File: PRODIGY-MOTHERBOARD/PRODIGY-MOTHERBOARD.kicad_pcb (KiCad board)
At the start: 2 copper layers, 160 x 115 mm, 252 parts, among them J10 Neopixel, J11 Can, J12 USB_A, J13 SPI_OUT, J14 MOTOR, J15 12V OUT, J16 RTD_PT100, J17 SERIAL, J18 I2C, J19 KEYPAD_MATRIX, J2 USB_C_Receptacle, J21 DM3BT-DSF-PEJS/C, J3 Conn_02x20_Odd_Even, J5 Barrel_Jack_MountingPin, J6 USB_C_Receptacle, J8 Conn_02x20_Odd_Even, J9 A_IN, Q1 BC850, Q2 DMP2045U-7, Q3 BC850, Q4 BS870, Q5 BC850, Q6 ALS-PDIC15-21B/TR8, SW1 SW_Push, SW2 SW_Push, SW3 SW_Push, SW4 SW_Push, SW5 SW_Push, SW6 SW_Push, U1 TPS22810DRV, U10 PCF8574, U11 HDC1080, U12 LIS2DH12TR, U13 TXS0108EPW, U15 CC56-12YWA, U16 PN5321A3HN_C1xx, U17 IP4252CZ16, U18 CR2013-MI2120, U19 SN74LVC1T45DBV, U2 TPS54331DR, U20 TSDP341xx, U22 MCP6021RT-E/OT, U23 LMP2011, U24 LM4125AIM5-2.5, U25 LMP2011, U26 LMP2011, U27 LMP2011, U3 TPS54331DR, U4 TJA1051T-E, U5 DRV8870DDA, U6 PCA9306DC, U7 PCA9306DC, U8 SN74LVC1T45DBV, U9 PCF8574

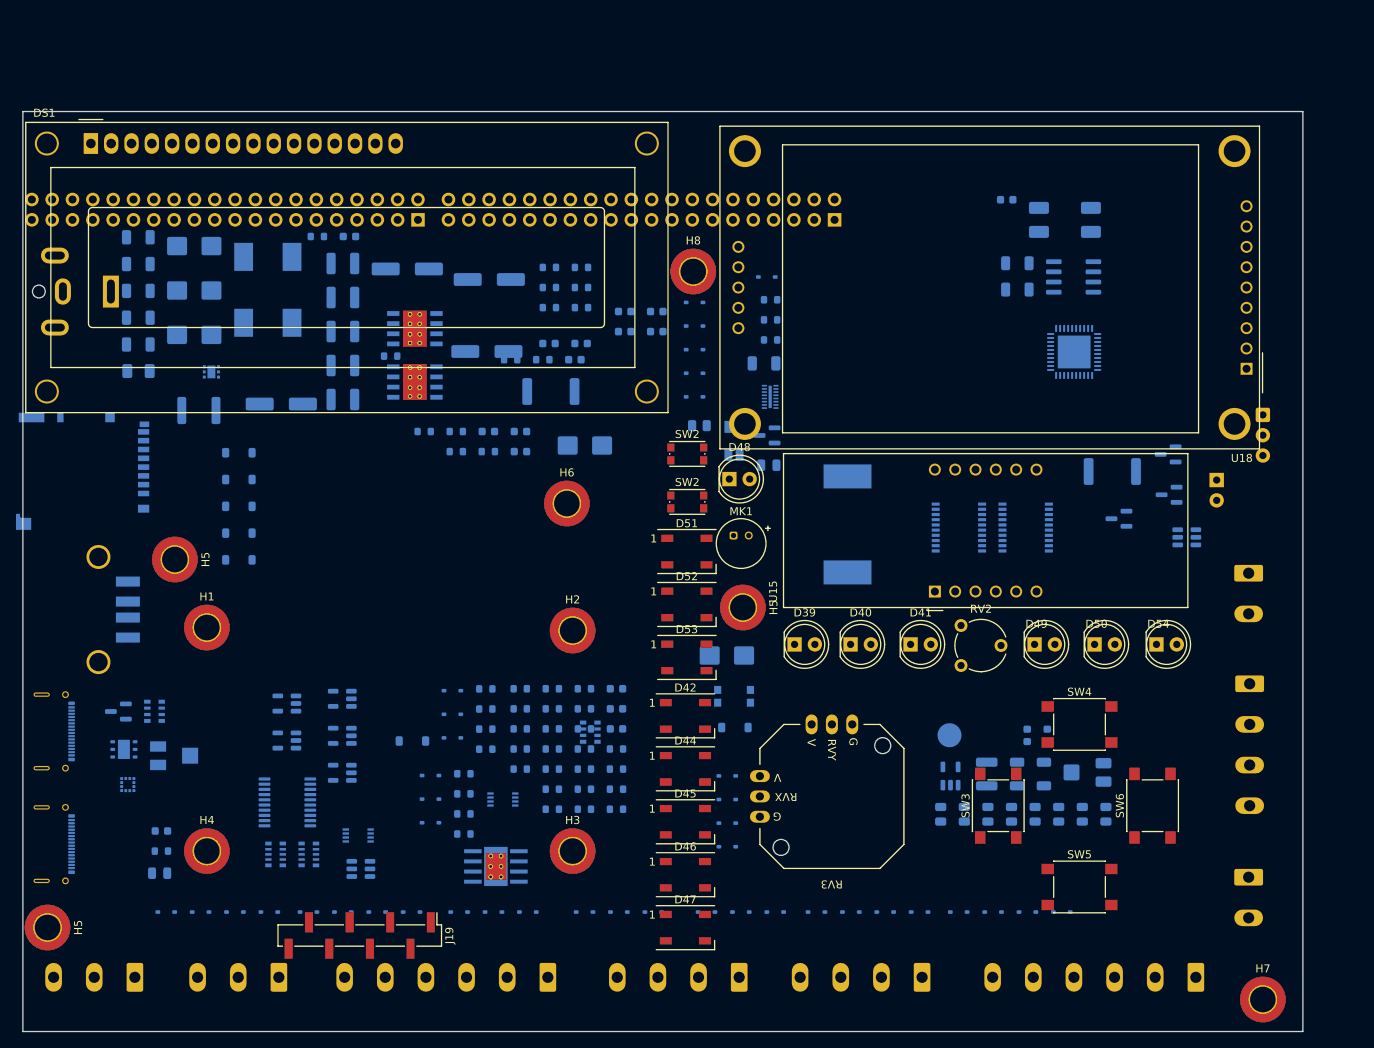
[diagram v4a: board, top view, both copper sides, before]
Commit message: MBT Schematic improved
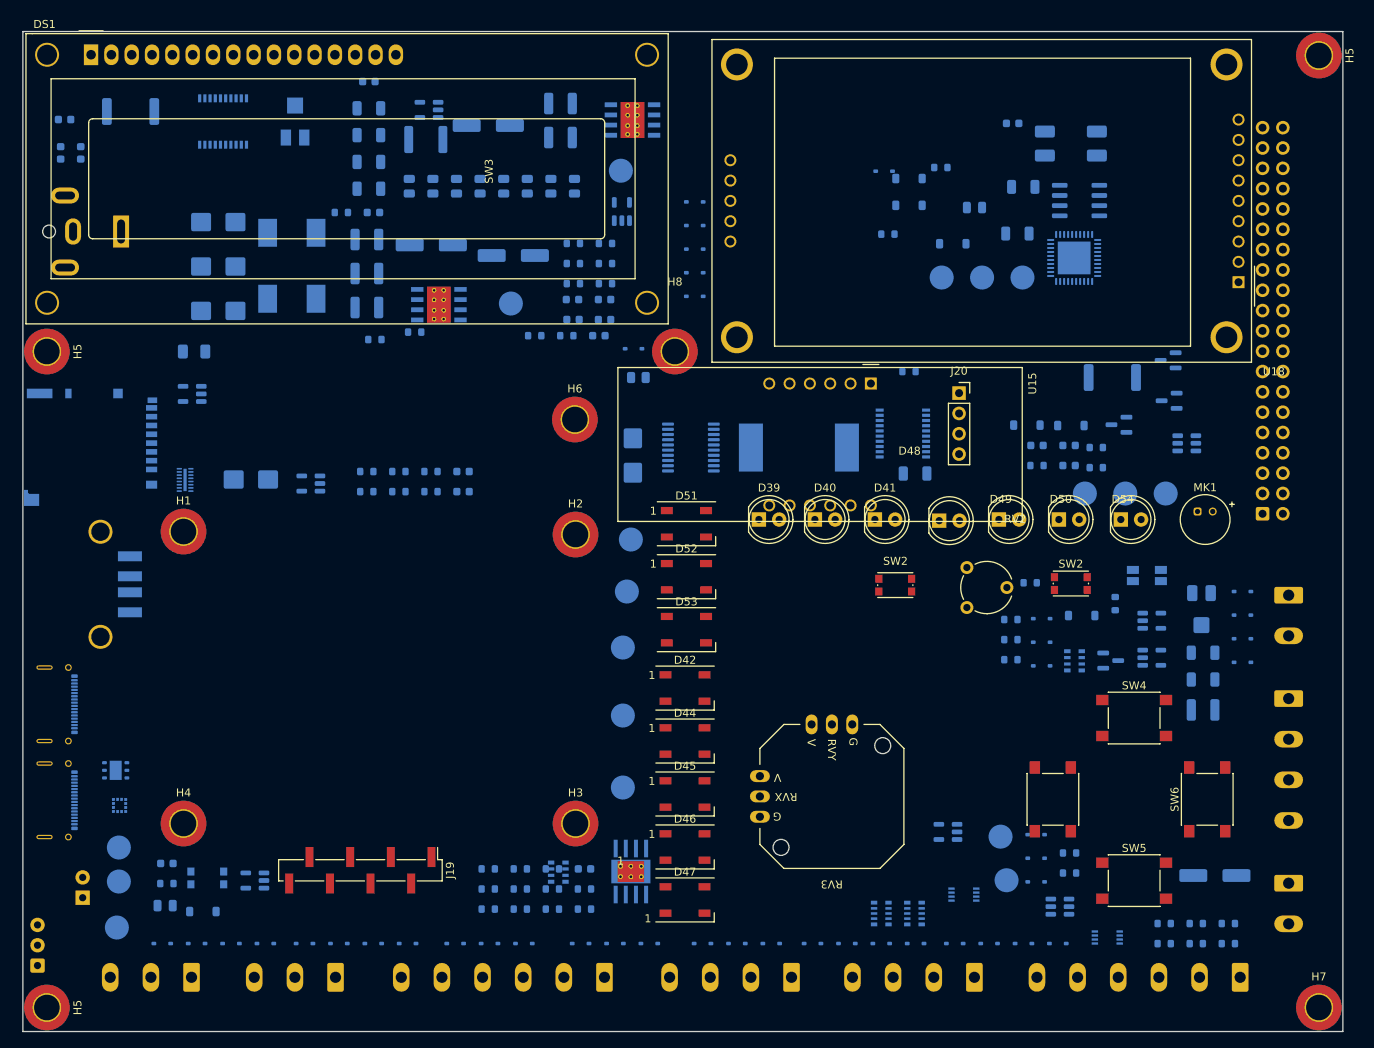
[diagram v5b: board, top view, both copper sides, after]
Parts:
- removed C3: 22nF, Capacitor_SMD:C_0603_1608Metric
- removed C65: 10uF, Capacitor_SMD:C_1206_3216Metric
- removed J21: DM3BT-DSF-PEJS/C, Connector_Card:microSD_HC_Hirose_DM3BT-DSF-PEJS
- removed J8: Conn_02x20_Odd_Even, Connector_PinHeader_2.54mm:PinHeader_2x20_P2.54mm_Horizontal
- removed Q2: DMP2045U-7, Package_TO_SOT_SMD:SOT-23
- removed R38, R39: 10k, Resistor_SMD:R_0603_1608Metric
- removed U17: IP4252CZ16, Package_SON:Nexperia_HUSON-16_USON-16-1EP_1.35x3.3mm_P0.4mm_EP0.4x2.8mm
- added C92: 100nF, Capacitor_SMD:C_0805_2012Metric, B.Cu at (186.9, 42.0)
- added J20: OLED, Connector_PinSocket_2.54mm:PinSocket_1x04_P2.54mm_Vertical, F.Cu at (185.0, 65.2)
- added J22: DM3BT-DSF-PEJS/C, Connector_Card:microSD_HC_Hirose_DM3BT-DSF-PEJS, B.Cu at (76.5, 72.0)
- added R88: 10k, Resistor_SMD:R_0603_1608Metric, B.Cu at (182.7, 37.0)
- added TP10: ~, TestPoint:TestPoint_Pad_D3.0mm, B.Cu at (190.2, 120.6)
- added TP11: ~, TestPoint:TestPoint_Pad_D3.0mm, B.Cu at (137.0, 83.0)
- added TP12: ~, TestPoint:TestPoint_Pad_D3.0mm, B.Cu at (191.0, 126.1)
- added TP13: ~, TestPoint:TestPoint_Pad_D3.0mm, B.Cu at (143.0, 97.0)
- added TP14: ~, TestPoint:TestPoint_Pad_D3.0mm, B.Cu at (129.0, 54.0)
- added TP15: ~, TestPoint:TestPoint_Pad_D3.0mm, B.Cu at (80.0, 122.0)
- added TP16: ~, TestPoint:TestPoint_Pad_D3.0mm, B.Cu at (80.0, 126.2)
- added TP2: ~, TestPoint:TestPoint_Pad_D3.0mm, B.Cu at (182.8, 50.8)
- added TP20: ~, TestPoint:TestPoint_Pad_D3.0mm, B.Cu at (143.0, 105.5)
- added TP21: ~, TestPoint:TestPoint_Pad_D3.0mm, B.Cu at (143.0, 114.5)
- added TP22: ~, TestPoint:TestPoint_Pad_D3.0mm, B.Cu at (144.0, 83.5)
- added TP3: ~, TestPoint:TestPoint_Pad_D3.0mm, B.Cu at (187.9, 50.8)
- added TP4: ~, TestPoint:TestPoint_Pad_D3.0mm, B.Cu at (192.9, 50.8)
- added TP5: ~, TestPoint:TestPoint_Pad_D3.0mm, B.Cu at (79.8, 132.0)
- added TP6: ~, TestPoint:TestPoint_Pad_D3.0mm, B.Cu at (200.8, 77.8)
- added TP7: ~, TestPoint:TestPoint_Pad_D3.0mm, B.Cu at (205.8, 77.8)
- added TP8: ~, TestPoint:TestPoint_Pad_D3.0mm, B.Cu at (210.8, 77.8)
- added TP9: ~, TestPoint:TestPoint_Pad_D3.0mm, B.Cu at (143.5, 90.0)
- added U29: IP4252CZ16, Package_SON:Nexperia_HUSON-16_USON-16-1EP_1.35x3.3mm_P0.4mm_EP0.4x2.8mm, B.Cu at (88.3, 76.0)
- added U30: RT9742AGJ5F, Package_TO_SOT_SMD:TSOT-23-5, B.Cu at (89.2, 65.3)
- C2: value 4.7uF -> 100nF; footprint Capacitor_SMD:C_1206_3216Metric -> Capacitor_SMD:C_0603_1608Metric
- C66: value 100nF -> 10uF; footprint Capacitor_SMD:C_0805_2012Metric -> Capacitor_SMD:C_1206_3216Metric
- J3: footprint Connector_PinHeader_2.54mm:PinHeader_2x20_P2.54mm_Horizontal -> Connector_IDC:IDC-Header_2x20_P2.54mm_Horizontal
- L2, L3: value 6.8 -> 6.8uH
- R40: value 100 -> DNP
- R5: value DNP -> 10k
- U1: value TPS22810DRV -> RT9742AGJ5F; footprint Package_SON:WSON-6-1EP_2x2mm_P0.65mm_EP1x1.6mm -> Package_TO_SOT_SMD:TSOT-23-5
- moved U20 167.9 mm to (69.8, 136.8), turned to 90 degrees
- moved H5 156.3 mm to (230.0, 23.0)
- moved D43 151.1 mm to (75.5, 128.3), turned to 90 degrees
- moved C85 141.1 mm to (75.2, 35.2)
- moved C86 141.1 mm to (72.7, 35.2)
- moved Q1 124.2 mm to (204.0, 98.6), turned to 0 degrees
- moved RN2 115.2 mm to (199.5, 98.7), turned to 0 degrees
- moved U9 112.4 mm to (93.0, 31.2), turned to -90 degrees
- moved C22 112.1 mm to (217.0, 125.5)
- moved J3 111.8 mm to (223.0, 80.3), turned to 0 degrees
- moved D58 104.2 mm to (199.0, 69.2)
- moved R72 102.8 mm to (136.9, 39.3)
- moved R73 102.8 mm to (134.0, 39.3)
- moved R75 102.8 mm to (128.1, 39.3)
- moved R76 102.8 mm to (125.2, 39.3)
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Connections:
- C2 pad 1: +5V -> /OUTPUTS/BREAKOUT_USB_VBUS
- C66 pad 1: /SPI/micro_SD/SD_VCC -> /SD/SD_VCC
- D66 pad 2: +3V3 -> +3.3VA
- Q6 pad 1: +3V3 -> +3.3VA
- Q6 pad 3: +3V3 -> +3.3VA
- R40 pad 2: /MCU/SPI_ENABLE_SD -> +3.3V
- R5 pad 1: Net-(U1-QOD) -> GND
- R5 pad 2: /OUTPUTS/BREAKOUT_USB_VBUS -> /MCU/USB_HOST_ENABLE
- RN3 pad 6: /SPI/CS_SD -> unconnected-(RN3-R5-Pad6)
- RV2 pad 3: +3V3 -> +3.3VA
- RV3 pad 1: +3V3 -> +3.3VA
- RV3 pad 4: +3V3 -> +3.3VA
- TH1 pad 1: +3V3 -> +3.3VA
- U1 pad 2: Net-(U1-QOD) -> GND
- U1 pad 3: Net-(U1-CT) -> /MCU/USB_HOST_FAULT
- U1 pad 4: GND -> /MCU/USB_HOST_ENABLE
- U1 pad 5: /MCU/USB_HOST_ENABLE -> +5V
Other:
- board size 160 x 115 mm -> 165 x 125 mm

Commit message: schematic v0.2 finalized
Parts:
- removed C92: 100nF, Capacitor_SMD:C_0805_2012Metric
- removed the H5 at (230.0, 23.0)
- removed the H5 at (71.0, 60.0)
- removed J22: DM3BT-DSF-PEJS/C, Connector_Card:microSD_HC_Hirose_DM3BT-DSF-PEJS
- removed Q6: ALS-PDIC15-21B/TR8, OptoDevice:Kingbright_KPS-3227
- removed R88: 10k, Resistor_SMD:R_0603_1608Metric
- removed TP20, TP21, TP22: ~, TestPoint:TestPoint_Pad_D3.0mm
- removed U29: IP4252CZ16, Package_SON:Nexperia_HUSON-16_USON-16-1EP_1.35x3.3mm_P0.4mm_EP0.4x2.8mm
- removed U30: RT9742AGJ5F, Package_TO_SOT_SMD:TSOT-23-5
- added C26: 100nF, Capacitor_SMD:C_0603_1608Metric, B.Cu at (99.6, 114.5)
- added C3: 100uF, Capacitor_SMD:CP_Elec_6.3x7.7, B.Cu at (97.0, 125.7)
- added C32: 47uF, Capacitor_SMD:CP_Elec_6.3x5.8, B.Cu at (110.2, 66.5)
- added C41: 10uF, Capacitor_SMD:C_0805_2012Metric, B.Cu at (90.1, 112.2)
- added C73: 4.7uF, Capacitor_SMD:C_0603_1608Metric, B.Cu at (99.6, 93.2)
- added C75: 4.7uF, Capacitor_SMD:C_0603_1608Metric, B.Cu at (99.6, 95.7)
- added C82: 1uF, Capacitor_SMD:C_0603_1608Metric, B.Cu at (119.7, 101.2)
- added C83: 100nF, Capacitor_SMD:C_0603_1608Metric, B.Cu at (119.7, 103.7)
- added C84: 100nF C0G, Capacitor_SMD:C_1206_3216Metric, B.Cu at (118.8, 93.6)
- added C90: 100nF, Capacitor_SMD:C_0805_2012Metric, B.Cu at (130.3, 113.2)
- added H10: MountingHole, MountingHole:MountingHole_3.2mm_M3_ISO7380_Pad_TopBottom, F.Cu at (230.0, 23.0)
- added H9: MountingHole, MountingHole:MountingHole_3.2mm_M3_ISO7380_Pad_TopBottom, F.Cu at (71.0, 60.0)
- added J21: DM3BT-DSF-PEJS/C, Connector_Card:microSD_HC_Hirose_DM3BT-DSF-PEJS, B.Cu at (76.5, 115.0)
- added Q2: BC850, Package_TO_SOT_SMD:SOT-23, B.Cu at (95.1, 94.3)
- added R38: 10k, Resistor_SMD:R_0603_1608Metric, B.Cu at (99.6, 98.2)
- added R39: 4.7k, Resistor_SMD:R_0603_1608Metric, B.Cu at (99.6, 100.7)
- added R69: 1k, Resistor_SMD:R_0805_2012Metric, B.Cu at (123.9, 93.4)
- added R70: 1k, Resistor_SMD:R_0805_2012Metric, B.Cu at (123.9, 96.3)
- added R71: 68k, Resistor_SMD:R_0805_2012Metric, B.Cu at (123.9, 99.3)
- added R85: DNP, Resistor_SMD:R_0603_1608Metric, B.Cu at (134.5, 113.0)
- added R86: 10k, Resistor_SMD:R_0603_1608Metric, B.Cu at (134.5, 115.5)
- added RN5: 10k, Resistor_SMD:R_Array_Convex_4x0603, B.Cu at (90.2, 106.3)
- added TP17: ~, TestPoint:TestPoint_Pad_D3.0mm, B.Cu at (120.0, 62.0)
- added TP18: ~, TestPoint:TestPoint_Pad_D3.0mm, B.Cu at (125.0, 62.0)
- added TP19: ~, TestPoint:TestPoint_Pad_D3.0mm, B.Cu at (130.1, 62.0)
- added U17: CR2013-MI2120, Display:CR2013-MI2120, F.Cu at (155.0, 30.3)
- added U21: MCP6021RT-E/OT, Package_TO_SOT_SMD:SOT-23-5, B.Cu at (119.1, 97.7)
- added U28: RT9742AGJ5F, Package_TO_SOT_SMD:TSOT-23-5, B.Cu at (134.0, 109.5)
- C11: value 100nF -> 10nF
- C13: value 10nF -> 1nF
- C14: value 1nF -> 4.7nF
- C15: value 4.7nF -> 47pF
- C16: value 47pF -> 39pF
- C17: value 39pF -> 100nF
- C19, C2: value 100nF -> 47uF; footprint Capacitor_SMD:C_0603_1608Metric -> Capacitor_SMD:C_1210_3225Metric
- C21: footprint Capacitor_SMD:C_1210_3225Metric -> Capacitor_SMD:CP_Elec_6.3x5.8
- C23: footprint Capacitor_SMD:CP_Elec_6.3x5.8 -> Capacitor_SMD:C_1210_3225Metric
- C4: value 100uF -> 100nF; footprint Capacitor_SMD:CP_Elec_6.3x7.7 -> Capacitor_SMD:C_0603_1608Metric
- C42: value 10uF -> 100nF; footprint Capacitor_SMD:C_0805_2012Metric -> Capacitor_SMD:C_0603_1608Metric
- C5: value 47uF -> 4.7uF; footprint Capacitor_SMD:C_1210_3225Metric -> Capacitor_SMD:C_1206_3216Metric
- C85: value 1uF -> 47uF; footprint Capacitor_SMD:C_0603_1608Metric -> Capacitor_SMD:C_1210_3225Metric
- C86: value 100nF -> 10uF; footprint Capacitor_SMD:C_0603_1608Metric -> Capacitor_SMD:C_1206_3216Metric
- C9: value 4.7uF -> 100nF; footprint Capacitor_SMD:C_1206_3216Metric -> Capacitor_SMD:C_0603_1608Metric
- D56: value 1N4148W -> SD05_SOD323; footprint Diode_SMD:D_SOD-123 -> Diode_SMD:D_SOD-323
- D57: value SD05_SOD323 -> 1N4148W; footprint Diode_SMD:D_SOD-323 -> Diode_SMD:D_SOD-123
- J10: value Neopixel -> RTD_PT100; footprint Connector_Phoenix_MSTB:PhoenixContact_MSTBA_2,5_3-G-5,08_1x03_P5.08mm_Horizontal -> Connector_Phoenix_MSTB:PhoenixContact_MSTBA_2,5_4-G-5,08_1x04_P5.08mm_Horizontal
- J16: value RTD_PT100 -> Neopixel; footprint Connector_Phoenix_MSTB:PhoenixContact_MSTBA_2,5_4-G-5,08_1x04_P5.08mm_Horizontal -> Connector_Phoenix_MSTB:PhoenixContact_MSTBA_2,5_3-G-5,08_1x03_P5.08mm_Horizontal
- Q3: value BC850 -> BS870
- Q4: value BS870 -> BC850
- Q5: value BC850 -> ALS-PDIC15-21B/TR8; footprint Package_TO_SOT_SMD:SOT-23 -> OptoDevice:Kingbright_KPS-3227
- R40: value DNP -> 1k
- R41: value 10k -> 100
- R42: value 4.7k -> 39
- R44: value 100 -> 1k
- R45: value 39 -> 1k
- R46, R48, R56, R60, R61: value 1k -> 10k
- R47, R72: value 1k -> 100
- R49: value 10k -> 22; footprint Resistor_SMD:R_0603_1608Metric -> Resistor_SMD:R_2512_6332Metric
- R50: value 100 -> 10k
- R52: value 22 -> 10k; footprint Resistor_SMD:R_2512_6332Metric -> Resistor_SMD:R_0603_1608Metric
- R54, R57, R58, R59: value 10k -> 1k
- R73: value 1k -> 220k
- R74: value 68k -> 220k
- R75: value 100 -> 220k
- R76: value 220k -> 1k
- RN3, RN4: footprint Resistor_SMD:R_Array_Convex_5x0603 -> Resistor_SMD:R_Array_Convex_4x0603
- TP1: value A1 -> ~
- TP16: value ~ -> A1
- U18: value CR2013-MI2120 -> SN74LVC1T45DBV; footprint Display:CR2013-MI2120 -> Package_TO_SOT_SMD:SOT-23-6; moved to B.Cu
- U19: value SN74LVC1T45DBV -> TSDP341xx; footprint Package_TO_SOT_SMD:SOT-23-6 -> OptoDevice:Vishay_MOLD-3Pin
- U22: value MCP6021RT-E/OT -> LMP2011; footprint Package_TO_SOT_SMD:SOT-23-5 -> Package_TO_SOT_SMD:TSOT-23-5
- U23: value LMP2011 -> LM4125AIM5-2.5; footprint Package_TO_SOT_SMD:TSOT-23-5 -> Package_TO_SOT_SMD:SOT-23-5
- U24: value LM4125AIM5-2.5 -> LMP2011; footprint Package_TO_SOT_SMD:SOT-23-5 -> Package_TO_SOT_SMD:TSOT-23-5
- U27: value LMP2011 -> IP4252CZ16; footprint Package_TO_SOT_SMD:TSOT-23-5 -> Package_SON:Nexperia_HUSON-16_USON-16-1EP_1.35x3.3mm_P0.4mm_EP0.4x2.8mm
- moved U18 110.0 mm to (124.7, 106.2), turned to 0 degrees
- moved TP16 71.8 mm to (82.0, 54.5)
- moved TP5 71.8 mm to (81.8, 60.2)
- moved TP15 44.8 mm to (85.5, 77.5)
- moved U12 41.9 mm to (80.5, 74.9)
- moved U11 41.9 mm to (80.0, 70.5)
- moved J2 34.6 mm to (71.5, 81.5)
- moved J6 34.6 mm to (71.5, 69.5)
- moved R45 26.0 mm to (93.5, 70.0)
- moved R46 26.0 mm to (93.5, 72.5)
- moved C76 26.0 mm to (97.5, 70.0)
- moved C78 26.0 mm to (97.5, 72.5)
- moved D3 18.3 mm to (81.8, 65.0)
- moved R53 18.3 mm to (100.3, 64.0)
- moved R54 18.3 mm to (100.3, 66.5)
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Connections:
- C10 pad 1: +12V -> +5V
- C11 pad 1: +5V -> Net-(U2-SS)
- C12 pad 1: Net-(U2-SS) -> Net-(U3-SS)
- C13 pad 1: Net-(U3-SS) -> Net-(U2-COMP)
- C13 pad 2: GND -> Net-(C13-Pad2)
- C14 pad 1: Net-(U2-COMP) -> Net-(U3-COMP)
- C15 pad 1: Net-(U3-COMP) -> Net-(U2-COMP)
- C15 pad 2: Net-(C15-Pad2) -> GND
- C16 pad 1: Net-(U2-COMP) -> Net-(U3-COMP)
- C17 pad 1: Net-(U3-COMP) -> Net-(U2-BOOT)
- C17 pad 2: GND -> Net-(D7-K)
- C18 pad 1: Net-(U2-BOOT) -> Net-(U3-BOOT)
- C18 pad 2: Net-(D7-K) -> Net-(D8-K)
- C19 pad 1: Net-(U3-BOOT) -> +3V3
- C19 pad 2: Net-(D8-K) -> GND
- C20 pad 1: +3V3 -> +5V
- C21 pad 1: +5V -> +3V3
- C22 pad 1: +3V3 -> +5V
- C23 pad 1: +5V -> +3V3
- C24 pad 1: +3V3 -> +5V
- C4 pad 1: +12V -> /OUTPUTS/BREAKOUT_USB_VBUS
- C5 pad 1: /OUTPUTS/BREAKOUT_USB_VBUS -> +12V
- C6 pad 1: +12V -> +5V
- C7 pad 1: +5V -> +12V
- C76 pad 1: /MCU/DIGITAL_BUTTON_IN_2 -> /MCU/DIGITAL_BUTTON_IN_1
- C8 pad 1: +12V -> +5V
- C85 pad 1: +3.3VA -> Net-(C84-Pad1)
- C85 pad 2: GND -> Net-(U21-+)
- C86 pad 1: +3.3VA -> Net-(U21--)
- C86 pad 2: GND -> Net-(C86-Pad2)
- C89 pad 1: Net-(U22--) -> /SD/SD_VCC
- C89 pad 2: Net-(C89-Pad2) -> GND
- C9 pad 1: +5V -> +12V
- D14 pad 2: /CAN/CAN_H -> /OUTPUTS/RTD_W1
- D15 pad 2: /OUTPUTS/BREAKOUT_NEOPIXEL_IN -> /OUTPUTS/RTD_W2
- D16 pad 2: /50Hz Filter/IN_P1+ -> /CAN/CAN_H
- D17 pad 2: /CAN/CAN_L -> /OUTPUTS/RTD_W3
- D18 pad 2: /50Hz Filter/IN_P1- -> /50Hz Filter/IN_P1+
- D19 pad 2: /SPI/CS_BREAKOUT -> /CAN/CAN_L
- D20 pad 2: /OUTPUTS/BREAKOUT_USB_VBUS -> /OUTPUTS/RTD_W4
- D21 pad 2: /MOTOR/MOTOR_OUT1_BREAKOUT_1 -> /50Hz Filter/IN_P1-
- D22 pad 2: /SPI/CLK -> /SPI/CS_BREAKOUT
- D23 pad 2: /MCU/USB_HOST_OUT_P+ -> /OUTPUTS/BREAKOUT_USB_VBUS
- D24 pad 2: /MCU/MOTOR_CC_IN_1 -> /MOTOR/MOTOR_OUT1_BREAKOUT_1
- D25 pad 2: /SPI/MISO -> /SPI/CLK
- D26 pad 2: /MCU/USB_HOST_OUT_P- -> /MCU/USB_HOST_OUT_P+
- D27 pad 2: /MCU/MOTOR_CC_IN_2 -> /MCU/MOTOR_CC_IN_1
- D28 pad 2: /SPI/MOSI -> /SPI/MISO
- D29 pad 2: /MOTOR/MOTOR_OUT2_BREAKOUT_1 -> /MCU/USB_HOST_OUT_P-
- D30 pad 2: /OUTPUTS/RTD_W1 -> /MCU/MOTOR_CC_IN_2
- D31 pad 2: +12V -> /SPI/CLK
- D32 pad 2: /OUTPUTS/RTD_W2 -> /MOTOR/MOTOR_OUT2_BREAKOUT_1
- D33 pad 2: /OUTPUTS/RTD_W3 -> +12V
- D34 pad 2: /OUTPUTS/RTD_W4 -> /OUTPUTS/BREAKOUT_NEOPIXEL_IN
- D56 pad 1: /MCU/DIGITAL_BUTTON_IN_2 -> GND
- D56 pad 2: Net-(D55-A2) -> Net-(D56-A2)
- D57 pad 1: GND -> Net-(D57-K)
- D57 pad 2: Net-(D57-A2) -> Net-(D56-A2)
- D58 pad 1: Net-(D58-K) -> /MCU/DIGITAL_BUTTON_IN_2
- D58 pad 2: Net-(D57-A2) -> Net-(D55-A2)
- J10 pad 1: /OUTPUTS/BREAKOUT_NEOPIXEL_IN -> /OUTPUTS/RTD_W1
- J10 pad 2: +5V -> /OUTPUTS/RTD_W2
- J10 pad 3: GND -> /OUTPUTS/RTD_W3
- J13 pad 4: /SPI/MOSI -> /SPI/CLK
- J16 pad 1: /OUTPUTS/RTD_W1 -> /OUTPUTS/BREAKOUT_NEOPIXEL_IN
- J16 pad 2: /OUTPUTS/RTD_W2 -> +5V
- J16 pad 3: /OUTPUTS/RTD_W3 -> GND
- Q3 pad 1: Net-(Q3-B) -> Net-(Q3-G)
- Q3 pad 3: Net-(D43-K) -> Net-(D54-K)
- Q4 pad 1: Net-(Q4-G) -> Net-(Q4-B)
- Q4 pad 3: Net-(D54-K) -> Net-(BZ1-+)
- Q5 pad 1: Net-(Q5-B) -> +3.3VA
- Q5 pad 2: GND -> /MCU/ANALOG_PHOTOTRANSISTOR
- Q5 pad 3: Net-(BZ1-+) -> +3.3VA
- R10 pad 1: Net-(C14-Pad2) -> Net-(C13-Pad2)
- R11 pad 1: Net-(C15-Pad2) -> Net-(C14-Pad2)
- R40 pad 1: Net-(R40-Pad1) -> GND
- R40 pad 2: +3.3V -> Net-(D41-K)
- R41 pad 1: GND -> /MCU/DIGITAL_IR_EMITTER
- R41 pad 2: Net-(D39-K) -> Net-(Q2-B)
- R42 pad 1: GND -> Net-(D43-A)
- R42 pad 2: Net-(D40-K) -> +3V3
- R43 pad 2: Net-(D41-K) -> Net-(D48-K)
- R44 pad 1: /MCU/DIGITAL_IR_EMITTER -> GND
- R44 pad 2: Net-(Q3-B) -> Net-(D49-K)
- R45 pad 1: Net-(D43-A) -> GND
- R45 pad 2: +3V3 -> Net-(D50-K)
- R46 pad 2: Net-(D48-K) -> /MCU/DIGITAL_HEATER_OUT
- R47 pad 1: GND -> /MCU/DIGITAL_HEATER_OUT
- R47 pad 2: Net-(D49-K) -> Net-(Q3-G)
- R48 pad 1: GND -> Net-(D54-A)
- R48 pad 2: Net-(D50-K) -> +12V
- R49 pad 1: GND -> Net-(F2-Pad2)
- R49 pad 2: /MCU/DIGITAL_HEATER_OUT -> Net-(D54-K)
- R50 pad 1: /MCU/DIGITAL_HEATER_OUT -> Net-(D55-A2)
- R50 pad 2: Net-(Q4-G) -> +3V3
- R51 pad 1: Net-(D54-A) -> Net-(D56-A2)
- R51 pad 2: +12V -> +3V3
- R52 pad 1: Net-(F2-Pad2) -> Net-(D56-A2)
- R52 pad 2: Net-(D54-K) -> Net-(D57-K)
- R53 pad 2: +3V3 -> /MCU/DIGITAL_BUTTON_IN_2
- R54 pad 1: Net-(D57-A2) -> /MCU/DIGITAL_BUZZER_OUT
- R54 pad 2: +3V3 -> Net-(Q4-B)
- R55 pad 1: Net-(D55-A2) -> Net-(D61-A2)
- R55 pad 2: /MCU/DIGITAL_BUTTON_IN_2 -> +3V3
- R56 pad 1: /MCU/DIGITAL_BUZZER_OUT -> Net-(D62-A2)
- R56 pad 2: Net-(Q5-B) -> +3V3
- R57 pad 1: Net-(D57-A2) -> /MCU/DIGITAL_RGB_R
- R57 pad 2: Net-(D58-K) -> Net-(D60-RA)
- R58 pad 1: Net-(D61-A2) -> /MCU/DIGITAL_RGB_G
- R58 pad 2: +3V3 -> Net-(D60-GA)
- R59 pad 1: Net-(D62-A2) -> /MCU/DIGITAL_RGB_B
- R59 pad 2: +3V3 -> Net-(D60-BA)
- R60 pad 1: /MCU/DIGITAL_RGB_R -> Net-(D61-A2)
- R60 pad 2: Net-(D60-RA) -> /MCU/DIGITAL_BUTTON_IN_3
- R61 pad 1: /MCU/DIGITAL_RGB_G -> Net-(D62-A2)
- R61 pad 2: Net-(D60-GA) -> /MCU/DIGITAL_BUTTON_IN_1
- R72 pad 1: /50Hz Filter/IN_P1+ -> Net-(R69-Pad2)
- R72 pad 2: Net-(R72-Pad2) -> Net-(C84-Pad1)
- R73 pad 1: /50Hz Filter/IN_P1- -> +3.3VA
- R73 pad 2: GND -> Net-(U21-+)
- R74 pad 1: Net-(R72-Pad2) -> Net-(U21-+)
- R75 pad 1: Net-(R72-Pad2) -> /50Hz Filter/ANALOG_BREAKOUT_OUT
- R75 pad 2: Net-(C87-Pad1) -> Net-(U21--)
- R76 pad 1: +3.3VA -> Net-(R76-Pad1)
- R76 pad 2: Net-(U22-+) -> GND
- RN3 pad 2: /MCU/SPI_CS_BREAKOUT -> /MCU/SPI_CS_NFC
- RN3 pad 3: unconnected-(RN3-R2-Pad3) -> /MCU/SPI_SCK
- RN3 pad 4: /MCU/SPI_CS_TFT -> /MCU/SPI_MISO
- RN3 pad 5: /MCU/SPI_CS_NFC -> /MCU/SPI_MOSI
- RN3 pad 6: unconnected-(RN3-R5-Pad6) -> (no net)
- RN3 pad 7: /MCU/SPI_CS_SEVENSEG -> (no net)
- RN3 pad 8: /MCU/SPI_MISO -> (no net)
- RN4 pad 1: +5V -> +3.3V
- RN4 pad 2: /SPI/MOSI -> /MCU/SPI_RST_NFC
- RN4 pad 3: /SPI/MISO -> /MCU/SPI_TFT_RESET
- RN4 pad 4: /SPI/CS_SEVENSEG -> /MCU/SPI_CS_BREAKOUT
- RN4 pad 5: /SPI/CS_BREAKOUT -> /MCU/SPI_CS_TFT
- RN4 pad 6: Net-(RN4-R5) -> (no net)
- RN4 pad 7: Net-(RN4-R6) -> (no net)
- RN4 pad 8: Net-(RN4-R7) -> (no net)
- RV4 pad 1: Net-(C89-Pad2) -> Net-(C86-Pad2)
- RV4 pad 2: Net-(R79-Pad1) -> Net-(R76-Pad1)
- SW4 pad 2: Net-(D57-A2) -> Net-(D56-A2)
- TP1 pad 1: /50Hz Filter/ANALOG_BREAKOUT_OUT -> /MCU/MCU_VREF
- TP10 pad 1: /MCU/ANALOG_PHOTOTRANSISTOR -> /MCU/ANALOG_POTENTIOMETER
- TP11 pad 1: /MCU/ANALOG_HEATER_TEMPERATURE -> /MCU/ANALOG_MICROPHONE
- TP12 pad 1: /MCU/ANALOG_MICROPHONE -> /MCU/ANALOG_PHOTOTRANSISTOR
- TP15 pad 1: /MCU/MCU_VREF -> /MCU/ANALOG_HEATER_TEMPERATURE
- TP16 pad 1: /CAN/CAN_EN -> /50Hz Filter/ANALOG_BREAKOUT_OUT
- TP2 pad 1: +12V -> Net-(F1-Pad1)
- TP3 pad 1: Net-(F1-Pad1) -> /OUTPUTS/BREAKOUT_USB_VBUS
- TP4 pad 1: +5V -> +3.3VA
- TP5 pad 1: +3V3 -> +12V
- TP6 pad 1: +3.3VA -> GND
- TP7 pad 1: /OUTPUTS/BREAKOUT_USB_VBUS -> +3V3
- TP8 pad 1: GND -> +5V
- TP9 pad 1: /MCU/ANALOG_POTENTIOMETER -> /CAN/CAN_EN
- U13 pad 12: Net-(RN4-R7) -> unconnected-(U13-B8-Pad12)
- U13 pad 13: Net-(RN4-R6) -> unconnected-(U13-B7-Pad13)
- U13 pad 14: Net-(RN4-R5) -> unconnected-(U13-B6-Pad14)
- U13 pad 20: /SPI/MOSI -> /SPI/CLK
- U18 pad 3: /MCU/SPI_CS_TFT -> /MCU/DIGITAL_NEOPIXEL_OUT
- U18 pad 4: /MCU/SPI_TFT_RESET -> Net-(D45-DIN)
- U18 pad 5: /MCU/SPI_TFT_DC -> GND
- U18 pad 6: /MCU/SPI_MOSI -> +5V
- U19 pad 1: +3V3 -> /MCU/DIGITAL_IR_RECEIVER
- U19 pad 3: /MCU/DIGITAL_NEOPIXEL_OUT -> +3V3
- U22 pad 1: /50Hz Filter/ANALOG_BREAKOUT_OUT -> /OUTPUTS/RTD_W1
- U22 pad 4: Net-(U22--) -> /OUTPUTS/RTD_W4
- U23 pad 1: /OUTPUTS/RTD_W1 -> unconnected-(U23-NC-Pad1)
- U23 pad 3: Net-(U23-+) -> unconnected-(U23-NC-Pad3)
- U23 pad 4: /OUTPUTS/RTD_W4 -> +3.3VA
- U23 pad 5: +3.3VA -> Net-(U22-+)
- U24 pad 1: unconnected-(U24-NC-Pad1) -> Net-(R78-Pad1)
- U24 pad 3: unconnected-(U24-NC-Pad3) -> /OUTPUTS/RTD_W2
- U24 pad 4: +3.3VA -> Net-(U24--)
- U24 pad 5: Net-(U23-+) -> +3.3VA
- U25 pad 3: /OUTPUTS/RTD_W2 -> Net-(U25-+)
- U25 pad 4: Net-(U25--) -> /OUTPUTS/RTD_W3
- U26 pad 1: Net-(R83-Pad2) -> /MCU/ANALOG_BREAKOUT_PT100
- U26 pad 4: /OUTPUTS/RTD_W3 -> Net-(U26--)
- U27 pad 1: /MCU/ANALOG_BREAKOUT_PT100 -> /SD/SD_DAT2
- U27 pad 2: GND -> /SD/SD_DAT3
- U27 pad 3: Net-(U27-+) -> /SD/SD_CMD
- U27 pad 4: Net-(U27--) -> /SD/SD_CLK
- U27 pad 5: +3.3VA -> /SD/SD_DAT0
